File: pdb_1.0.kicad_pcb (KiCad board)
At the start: 4 copper layers, 127.7 x 81.9 mm, 63 parts, among them J1 Screw_Terminal_01x02, J10 Screw_Terminal_01x02, J2 Screw_Terminal_01x02, J3 Screw_Terminal_01x02, J7 Screw_Terminal_01x02, J8 Screw_Terminal_01x02, J9 Screw_Terminal_01x02, Q1 BSC340N08NS3G, Q2 BSC340N08NS3G, Q3 BSC340N08NS3G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

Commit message: chip layout, still need finalize a few peices and check for stock
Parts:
- added C1: 100u, Capacitor_SMD:C_Elec_10x10.2, F.Cu at (110.3, 86.6)
- added C26: 0.1u, Capacitor_SMD:C_1206_3216Metric, F.Cu at (165.7, 66.1)
- added C27: 0.1u, Capacitor_SMD:C_1206_3216Metric, F.Cu at (162.3, 66.1)
- added C28: 0.1u, Capacitor_SMD:C_1206_3216Metric, F.Cu at (84.0, 112.9)
- added C29: 0.1u, Capacitor_SMD:C_1206_3216Metric, F.Cu at (84.0, 116.1)
- added C30: 0.1u, Capacitor_SMD:CP_Elec_5x5.4, F.Cu at (171.5, 91.5)
- added R23: 1M, Capacitor_SMD:C_0805_2012Metric, F.Cu at (167.2, 103.7)
- added R24: 1M, Capacitor_SMD:C_0805_2012Metric, F.Cu at (120.0, 112.8)
- C14, C8: value 25n -> 50n
- C18: footprint Capacitor_SMD:C_1206_3216Metric -> Capacitor_SMD:CP_Elec_5x5.4
- C19: value 62p -> 65n
- C20: value 5.6p -> 9.9n
- C21: value 1800p -> 163n
- C22: value 27p -> 25n
- L1: value 47u -> 56u; footprint Inductor_SMD:L_Wuerth_HCF-2013 -> Inductor_SMD:L_Wuerth_HCI-2212
- L2: value 14u -> 33u; footprint Inductor_SMD:L_Wuerth_HCF-2013 -> Inductor_SMD:L_Wuerth_HCI-1890
- R1, R10: value 46.2k -> 374k
- R16: value 17m -> 15m
- R17, R8: value 60.4k -> 402k
- R18: value 7.87k -> 62k
- R19: value 442k -> 674k
- R20: value 46.4k -> 268k
- R6: value 28m -> 22m
- R9: value 2.67k -> 22.6k
- moved J3 78.6 mm to (162.7, 60.4), turned to 0 degrees
- moved C17 67.9 mm to (154.5, 66.0), turned to -90 degrees
- moved C25 62.8 mm to (158.5, 66.1), turned to -90 degrees
- moved D1 60.6 mm to (135.3, 115.0)
- moved C5 54.5 mm to (172.9, 73.5), turned to 90 degrees
- moved C24 43.9 mm to (170.9, 87.1), turned to 180 degrees
- moved C18 34.9 mm to (104.7, 122.5), turned to -90 degrees
- moved R14 34.5 mm to (163.8, 99.5), turned to 90 degrees
- moved C19 31.7 mm to (115.5, 107.5), turned to 180 degrees
- moved R13 30.3 mm to (161.3, 99.5), turned to 90 degrees
- moved R11 29.9 mm to (162.8, 108.8), turned to 180 degrees
- moved R12 29.9 mm to (162.8, 106.6), turned to 180 degrees
- moved C23 28.0 mm to (99.0, 123.2), turned to -90 degrees
- moved C16 28.0 mm to (163.6, 103.7), turned to -90 degrees
- moved C20 27.6 mm to (117.0, 110.8), turned to -90 degrees
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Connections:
- D1 pad 1: /BSTVcc -> /BOOST
- D1 pad 2: /BOOST -> /BSTVcc
- D1 pad 3: /BSTVcc -> (no net)
- D2 pad 1: /BSTVcc_7v -> /BOOST_7v
- D2 pad 2: /BOOST_7v -> /BSTVcc_7v
- D2 pad 3: /BSTVcc_7v -> (no net)
- U1 pad 18: /INTVcc -> Net-(U1-PGOOD)
- U1 pad 2: /INTVcc -> GND
- U2 pad 18: /INTVcc_7v -> Net-(U2-PGOOD)
- U2 pad 2: /INTVcc_7v -> GND
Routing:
- net +7V: track 0.00 -> 50.4 mm, vias 0 -> 6
- net +19V: track 0.00 -> 47.6 mm, vias 0 -> 3
- net +24V19: track 0.00 -> 46.7 mm, vias 0 -> 3
- net /BG: track 0.00 -> 41.6 mm, vias 0 -> 5
- net /INTVcc: track 3.87 -> 41.3 mm, vias 0 -> 4
- net /sense+7v: track 0.00 -> 33.1 mm, vias 0 -> 2
- net /TG_7v: track 0.00 -> 25.8 mm
- net /sense+: track 0.00 -> 22.4 mm, vias 0 -> 2
- net /SW: track 0.00 -> 21.4 mm
- net /TG: track 0.00 -> 11.2 mm, vias 0 -> 4
- net /Vfb: track 0.00 -> 10.6 mm
- net Net-(U2-TGUP): track 0.00 -> 10.1 mm
- net Net-(U2-ITH): track 0.00 -> 9.12 mm
- net /Vfb_7v: track 0.00 -> 8.44 mm
- net /SW_7v: track 0.00 -> 8.21 mm
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- added copper zone on F.Cu, net /sense+

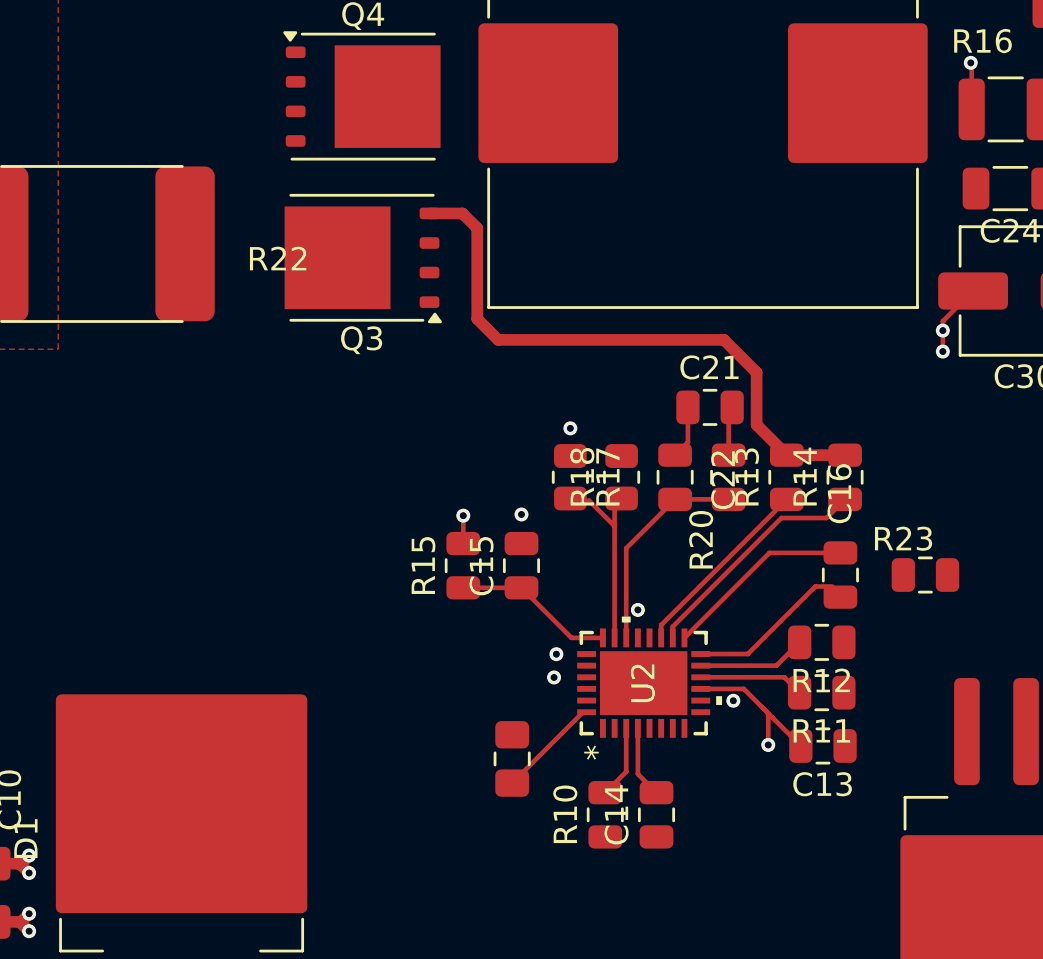
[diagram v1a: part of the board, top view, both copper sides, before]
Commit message: some trace done
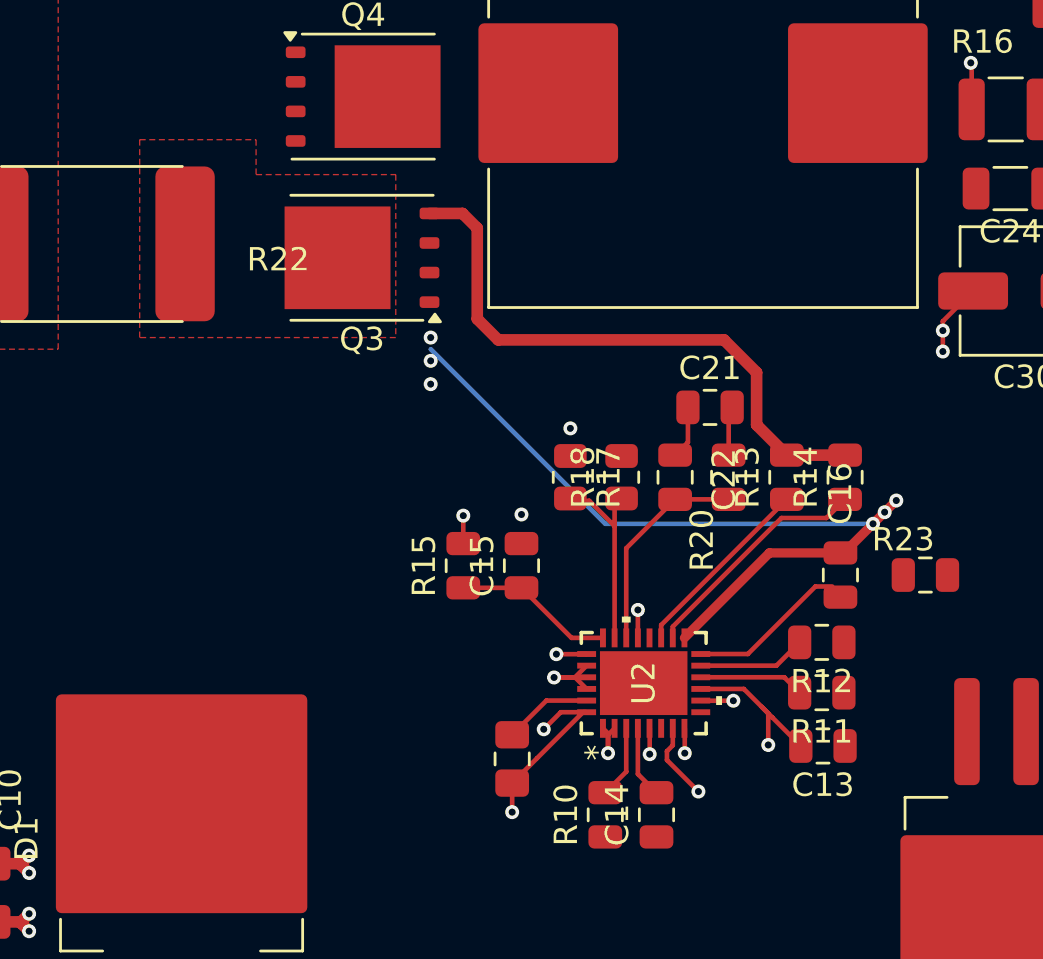
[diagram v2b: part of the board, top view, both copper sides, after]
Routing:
- net /SW_7v: track 8.21 -> 33.7 mm, vias 0 -> 6
- net /INTVcc_7v: track 7.05 -> 31.6 mm, vias 3 -> 4
- net GND: track 0.00 -> 9.07 mm, vias 0 -> 2
- net +24V7: track 4.46 -> 11.2 mm, vias 0 -> 3
- net +7V: track 50.4 -> 53.1 mm
- added copper zone on F.Cu, net +24V7

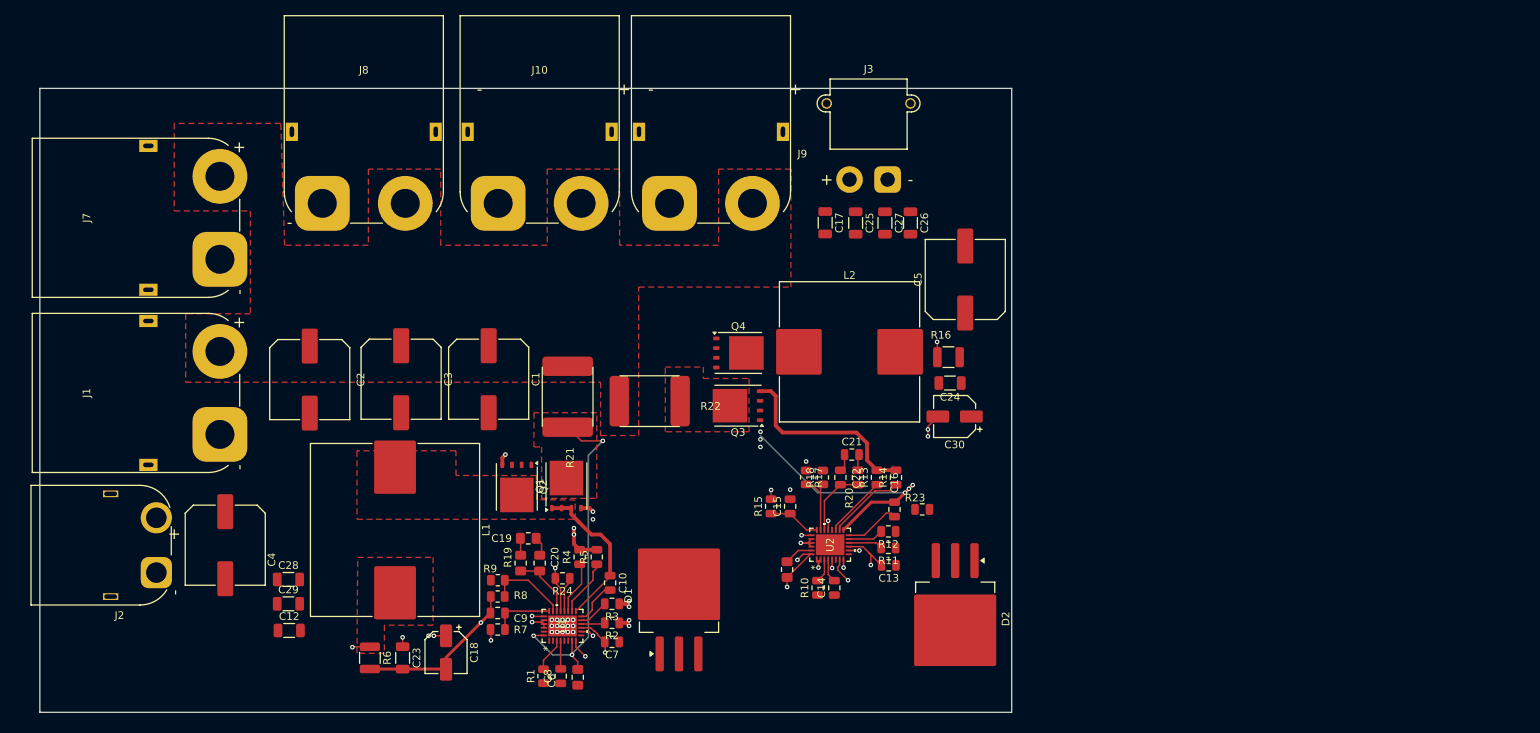
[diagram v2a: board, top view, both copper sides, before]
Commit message: finshed all connection, need double checking datasheet and componenet availaibility on JLC
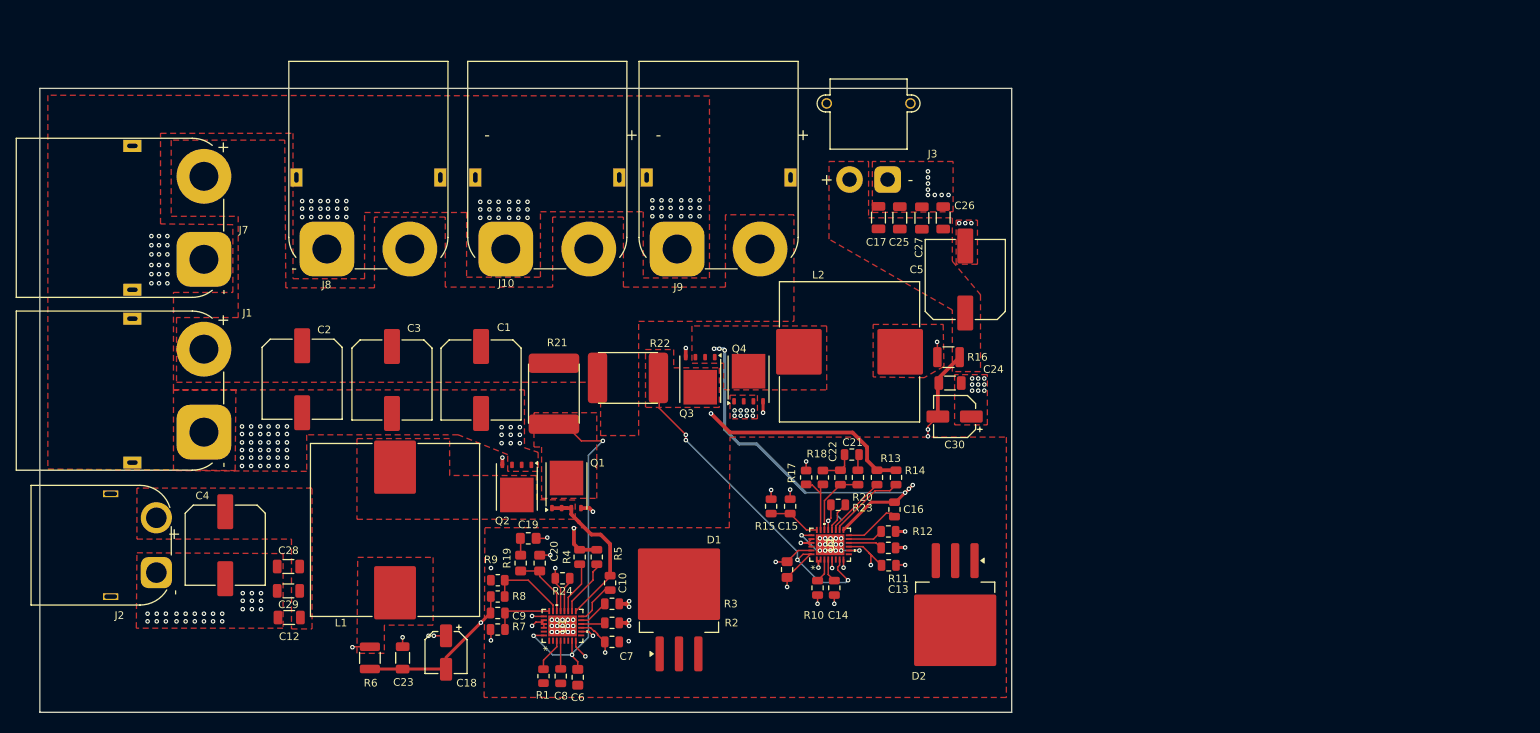
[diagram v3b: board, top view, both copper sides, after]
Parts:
- moved R23 11.1 mm to (156.2, 103.1), turned to 180 degrees
- moved C17 7.03 mm to (161.5, 65.4)
- moved J10 6.08 mm to (112.5, 69.5)
- moved J9 6.08 mm to (135.1, 69.5)
- moved Q3 6.05 mm to (138.1, 86.6), turned to -90 degrees
- moved J8 6.03 mm to (89.0, 69.5)
- moved C25 5.84 mm to (164.3, 65.4)
- moved C27 4.89 mm to (167.2, 65.4)
- moved C26 4.35 mm to (170.0, 65.4)
- moved R22 4.17 mm to (128.6, 87.1)
- moved Q4 3.70 mm to (144.4, 86.6), turned to 90 degrees
- moved J1 2.12 mm to (72.9, 93.5)
- moved J7 2.10 mm to (72.9, 70.8)
- moved R21 1.84 mm to (118.2, 88.5)
- moved C28 1.70 mm to (84.0, 111.2)
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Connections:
- C1 pad 2: GNDPWR -> GNDA
- C11 pad 1: GND -> GNDA
- C12 pad 1: GNDPWR -> GNDA
- C13 pad 1: GND -> GNDA
- C14 pad 1: GND -> GNDA
- C18 pad 1: GNDPWR -> GNDA
- C2 pad 2: GNDPWR -> GNDA
- C23 pad 1: GNDPWR -> GNDA
- C24 pad 1: GNDPWR -> GNDA
- C25 pad 1: GNDPWR -> GNDA
- C26 pad 1: GNDPWR -> GNDA
- C27 pad 1: GNDPWR -> GNDA
- C28 pad 1: GNDPWR -> GNDA
- C29 pad 1: GNDPWR -> GNDA
- C3 pad 2: GNDPWR -> GNDA
- C30 pad 1: GNDPWR -> GNDA
- C4 pad 2: GNDPWR -> GNDA
- C5 pad 2: GNDPWR -> GNDA
- C6 pad 1: GND -> GNDA
- C7 pad 1: GND -> GNDA
- C8 pad 1: GND -> GNDA
- J1 pad 1: GNDPWR -> GNDA
- J10 pad 1: GNDPWR -> GNDA
- J2 pad 1: GNDPWR -> GNDA
- J3 pad 1: GNDPWR -> GNDA
- J7 pad 1: GNDPWR -> GNDA
- J8 pad 1: GNDPWR -> GNDA
- J9 pad 1: GNDPWR -> GNDA
- Q2 pad 1: GNDPWR -> GNDA
- Q2 pad 2: GNDPWR -> GNDA
- Q2 pad 3: GNDPWR -> GNDA
- Q4 pad 1: GNDPWR -> GNDA
- Q4 pad 2: GNDPWR -> GNDA
- Q4 pad 3: GNDPWR -> GNDA
- R1 pad 1: GND -> GNDA
- R10 pad 1: GND -> GNDA
- U1 pad 1: GND -> GNDA
- U1 pad 2: GND -> GNDA
- U1 pad 27: GND -> GNDA
- U1 pad 29: GNDPWR -> GNDA
- U1 pad 5: GND -> GNDA
- U2 pad 1: GND -> GNDA
- U2 pad 2: GND -> GNDA
- U2 pad 27: GND -> GNDA
- U2 pad 29: GNDPWR -> GNDA
- U2 pad 5: GND -> GNDA
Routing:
- net +24V7: track 11.2 -> 50.7 mm, vias 3 -> 5
- net /BG_7v: track 0.00 -> 31.4 mm, vias 0 -> 3
- net /INTVcc: track 41.3 -> 16.6 mm
- net GNDA: track 4.79 -> 25.1 mm, vias 0 -> 215
- net /SW_7v: track 33.7 -> 50.6 mm
- net /INTVcc_7v: track 31.6 -> 16.3 mm
- net /TG_7v: track 25.8 -> 39.6 mm, vias 0 -> 2
- net GND: track 9.07 -> 0.00 mm, vias 2 -> 0
- net Net-(U2-PGOOD): track 0.00 -> 4.87 mm
- net GNDPWR: track 3.52 -> 0.00 mm, vias 18 -> 0
- net +7V: track 53.1 -> 54.9 mm
- net /TG: vias 4 -> 2
- added copper zone on F.Cu, net +19V
- added copper zone on In2.Cu, net +19V
- added copper zone on F.Cu, net +7V
- added copper zone on In2.Cu, net +7V
- added copper zone on In2.Cu, net /INTVcc
- added copper zone on In2.Cu, net /INTVcc_7v
- added copper zone on F.Cu, net /SW_7v
- added copper zone on F.Cu, net /sense+7v
- added copper zone on F.Cu, net GNDA
- added copper zone on In1.Cu, net GNDA
- removed copper zone on In1.Cu, net GNDPWR
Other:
- board text added: "U1"
